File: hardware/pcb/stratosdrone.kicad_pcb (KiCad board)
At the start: 4 copper layers, 36 x 70 mm, 115 parts, among them J1 BATT_PH2, J10 DBG, J11 C6DBG, J2 USB-C-16P, J3 FLOW_HDR, J4 CAM_FFC15, J5 MOTOR1, J6 MOTOR2, J7 MOTOR3, J8 MOTOR4, J9 EXP, Q1 AO3400A, Q2 AO3400A, Q3 AO3400A, Q4 AO3400A, SW1 RESET, SW2 BOOT, U1 ESP32-P4NRW32, U10 TLV62569DBVR, U2 W25Q128JVSIQ, U3 ESP32-C6-MINI-1, U4 TP4056-42-ESOP8, U5 SY8089AAAC, U6 ICM-42688-P, U7 SPL06-001, U8 VL53L1X, U9 PMW3901MB, Y1 40MHz

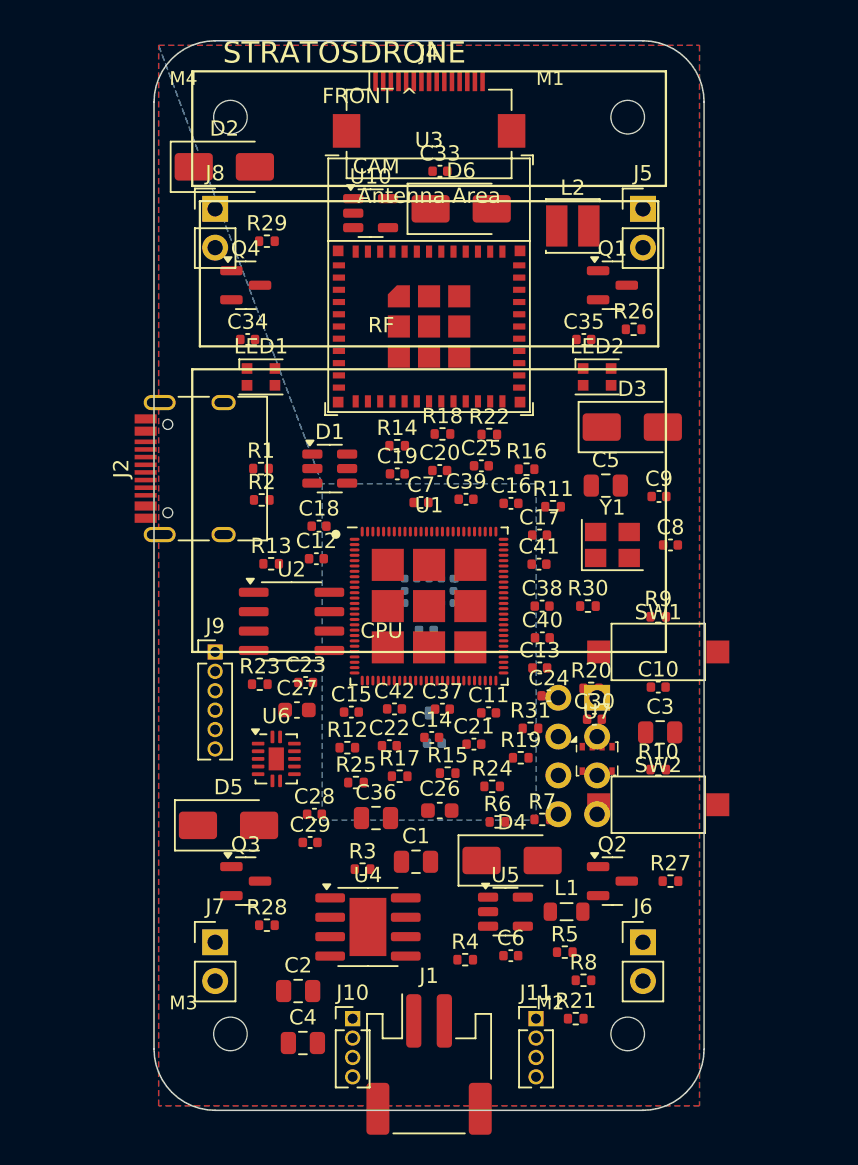
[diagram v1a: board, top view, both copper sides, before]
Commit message: hardware/pcb: fix two router-blocking footprint bugs + add autoroute pipeline
Two real bugs that broke Specctra DSN export and any autorouter, found while
building the AI-assisted routing flow:

1. Mounting holes had EMPTY references. gen_pcb.py created the 4 corner M2 NPTH
   holes as footprints with no reference designator; Specctra export aborts when
   multiple components share an empty ref, so ExportSpecctraDSN() returned False
   with no error. Now MH1..MH4 with a real footprint id, excluded from BOM/CPL.

2. U9 (PMW3901) placeholder had all 8 pads stacked at (0,0) on 8 DIFFERENT nets
   (GND/3V3/SPI_*/CS_FLOW) — a hard short that poisoned the maze router for those
   nets. Replaced with a spread 2x4 DFN-style land (0.8mm pitch); verified zero
   different-net pad overlaps remain board-wide.

New routing infrastructure:
- scripts/route_board.py: export Specctra DSN (drops outer F.Cu/B.Cu pours so
  signal layers are free, marks inner In1/In2 as power planes, optional
  power-net strip), drive Freerouting headless under xvfb, import the routed
  SES back with a self-contained parser (correct um scale + Specctra Y-flip),
  and stitch power pads to their planes.
- ROUTING.md: method + online-AI (DeepPCB) and Windows-Freerouting fallbacks.
- stratosdrone.dsn: committed handoff so the board can be routed anywhere.

Board regenerated; check_consistency passes. Signal autoroute itself is still
in progress (see ROUTING.md); these fixes unblock it on every router.

Co-Authored-By: Claude Opus 4.8 <noreply@anthropic.com>
Claude-Session: https://claude.ai/code/session_011szEEHZ8KTTsZmGFgY6Cjw
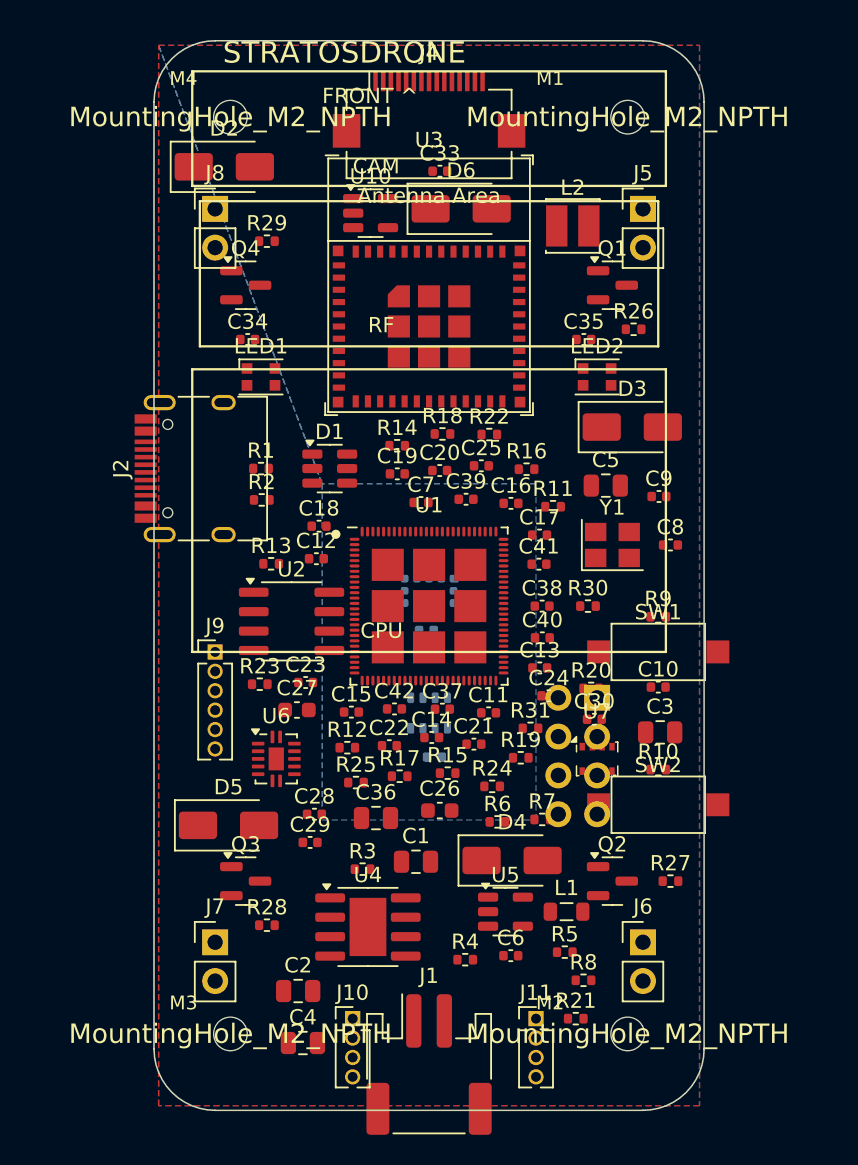
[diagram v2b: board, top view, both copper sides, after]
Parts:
- removed ? (x4): , 
- added MH1: MountingHole_M2_NPTH, MountingHole:MountingHole_2.2mm_M2, F.Cu at (5.00, 5.00)
- added MH2: MountingHole_M2_NPTH, MountingHole:MountingHole_2.2mm_M2, F.Cu at (5.00, 65.0)
- added MH3: MountingHole_M2_NPTH, MountingHole:MountingHole_2.2mm_M2, F.Cu at (31.0, 5.00)
- added MH4: MountingHole_M2_NPTH, MountingHole:MountingHole_2.2mm_M2, F.Cu at (31.0, 65.0)
- moved C32 0.91 mm to (18.3, 46.9)

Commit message: hardware/pcb: apply AI signal autoroute (Freerouting 1.9), ~89% of signals
Drove Freerouting 1.9.0 headless (xvfb) via scripts/route_board.py on the
de-bugged board and imported the result: 295 signal track segments on
F.Cu/B.Cu (stratosdrone.ses, committed). The self-contained SES importer was
fixed to the correct Specctra scale (0.1um/unit) and Y-axis flip, verified
against known pad positions.

State: signal nets ~89% routed; the rest is finished in KiCad (see ROUTING.md
and KNOWN_GAPS item 1):
- fill the 4 copper zones (hotkey B) -> connects same-layer GND/VBAT pads;
- add cross-layer power stitch vias (3V3 -> In2 plane) — connect_power() does
  a first pass but headless zone-fill can't replicate KiCad's GUI connectivity
  reliably, so KiCad's fill is authoritative;
- route the few remaining ratsnest signals; re-export gerbers.

Why not 100% here: this dense 36x70mm 2-signal-layer board caps at ~62% of
all connections per autorouter pass in this sandbox (FR1.9 best; FR2.1 weaker;
both plateau). A full clean route wants more compute — route the committed
stratosdrone.dsn on DeepPCB.ai (cloud AI) or Windows Freerouting and re-import
with `route_board.py --skip-route`.

`make board` regenerates the UNROUTED board; re-apply with
`route_board.py --skip-route`. check_consistency passes.

Co-Authored-By: Claude Opus 4.8 <noreply@anthropic.com>
Claude-Session: https://claude.ai/code/session_011szEEHZ8KTTsZmGFgY6Cjw
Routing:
- net VBAT: track 0.00 -> 130.0 mm
- net GND: track 0.00 -> 62.7 mm
- net SPI_MISO: track 0.00 -> 26.1 mm, vias 0 -> 1
- net VBUS: track 0.00 -> 24.9 mm
- net SPI_MOSI: track 0.00 -> 23.6 mm, vias 0 -> 1
- net LED_D12: track 0.00 -> 21.8 mm, vias 0 -> 2
- net M3_GATE: track 0.00 -> 21.2 mm
- net I2C_SCL: track 0.00 -> 19.7 mm
- net SPI_SCLK: track 0.00 -> 19.3 mm, vias 0 -> 1
- net I2C_SDA: track 0.00 -> 17.1 mm
- net SDIO_D1: track 0.00 -> 16.8 mm
- net M1_D: track 0.00 -> 15.9 mm
- net FB_DCDC: track 0.00 -> 14.0 mm
- net M2_D: track 0.00 -> 13.0 mm
- net FB3V3: track 0.00 -> 12.1 mm
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
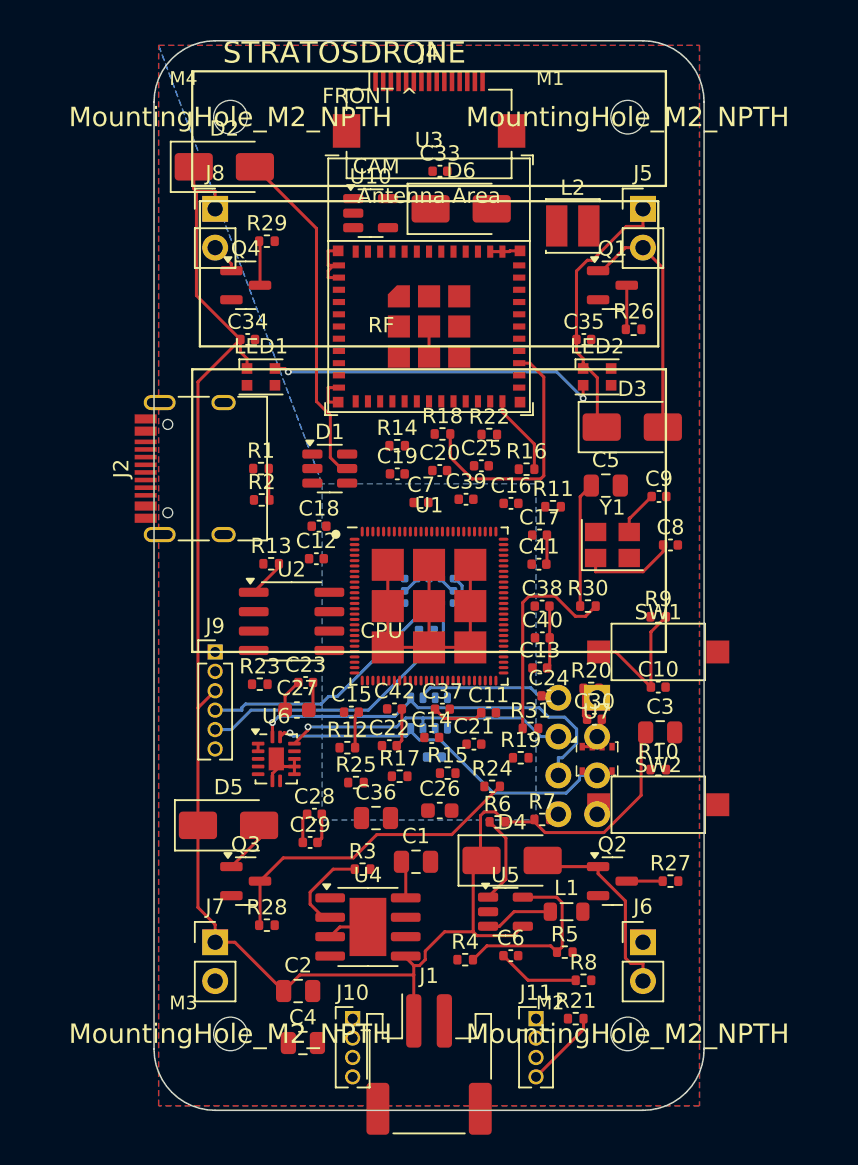
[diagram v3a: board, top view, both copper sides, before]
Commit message: hardware/pcb: fix component placement — nothing off-board, no overlaps
Opening the board in KiCad showed parts hanging off the outline (USB-C J2,
the reset/boot switches SW1/SW2) and a congested bottom-right cluster. Root
cause: phase-1 anchors in the PLACE table were positioned by hand with no
boundary/overlap check, and the phase-3 repair pass explicitly skips anything
in PLACE — so off-board or colliding *major* parts were never corrected.

Placement fixes (PLACE table):
- SW1/SW2 (9.3mm slide switches) rotated 90° and moved to a clear vertical
  column on the right edge — they no longer hang 1.6mm off the edge nor
  collide with U7/J3 and their gate resistors (the bottom-right mess).
- J2 USB-C moved right so all contacts sit on-board (the 90° rotation made the
  1.45mm contact fingers straddle the x=0 edge -> off-board copper).
- J1 battery JST pulled up off the bottom edge; J10/J11 UART pads likewise.
- U3 (ESP32-C6) spaced from the camera FFC; U4/U5/L1 nudged for clearance.

Engine: add assert_placement(), run at the end of main(), which loads the
saved board and reports any pad outside the outline (hard error -> exit 2) and
significant same-side courtyard overlaps (warnings). `make board` now fails if
placement regresses off-board.

Result: all 111 footprints inside the 36x70 outline, zero same-side pad
overlaps, tightest body gap 0.28mm (JLCPCB-safe). Remaining courtyard warnings
are oversized module IPC courtyards (ESP32-C6/camera-FFC/USB-C) with >=0.28mm
real clearance.

Note: moving parts invalidates the previous autoroute; tracks are re-routed on
the corrected placement in a follow-up commit. stratosdrone.dsn re-exported.

Co-Authored-By: Claude Opus 4.8 <noreply@anthropic.com>
Claude-Session: https://claude.ai/code/session_011szEEHZ8KTTsZmGFgY6Cjw
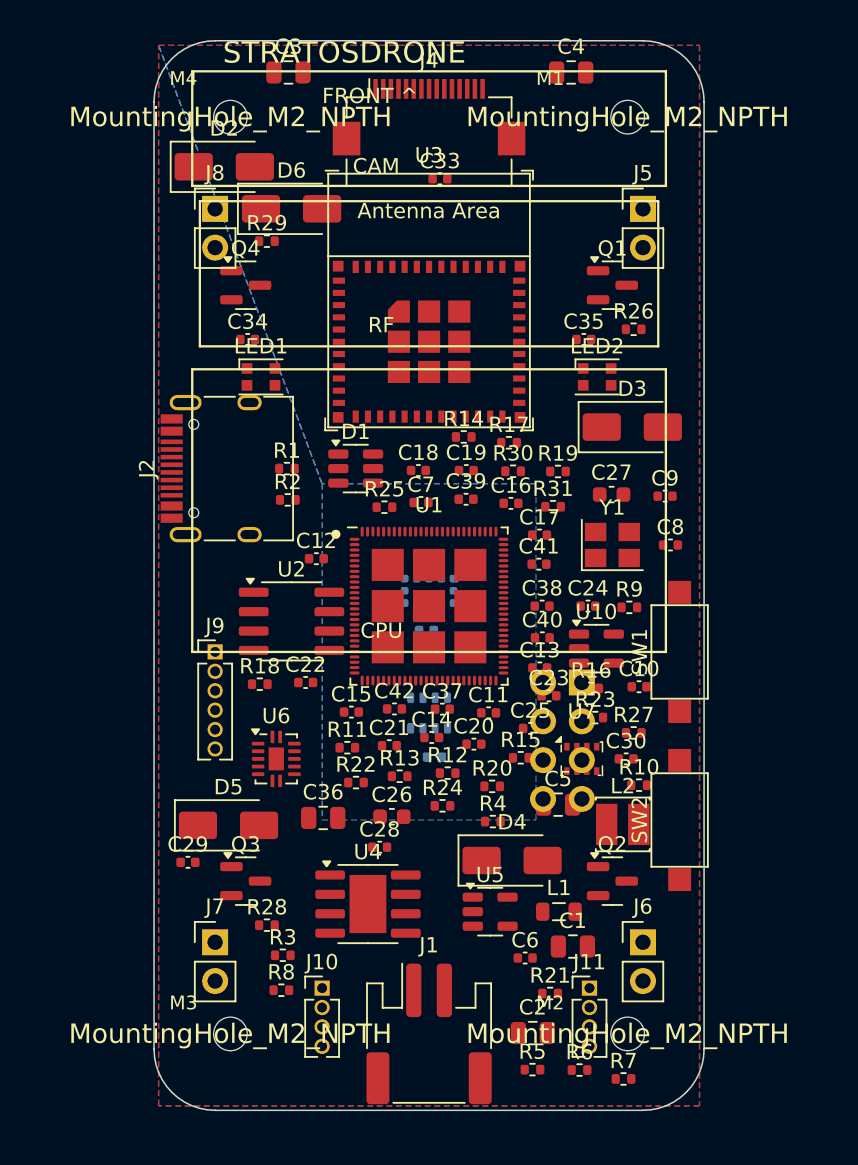
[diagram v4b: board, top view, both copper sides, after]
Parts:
- moved C4 65.9 mm to (27.3, 2.08)
- moved C3 49.6 mm to (8.80, 2.08)
- moved L2 39.3 mm to (30.7, 51.3)
- moved U10 32.1 mm to (29.0, 39.8)
- moved C27 25.0 mm to (29.9, 29.7)
- moved R22 24.4 mm to (13.2, 48.5)
- moved R17 23.0 mm to (23.2, 26.3)
- moved R23 22.1 mm to (28.9, 44.3)
- moved C5 21.1 mm to (26.4, 50.0)
- moved R11 20.7 mm to (12.7, 46.3)
- moved R18 20.3 mm to (6.92, 42.1)
- moved R8 19.8 mm to (8.33, 62.1)
- moved R19 18.9 mm to (26.4, 28.2)
- moved R25 18.1 mm to (15.1, 30.5)
- moved C20 18.0 mm to (20.9, 46.0)
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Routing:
- net VBAT: track 130.0 -> 0.00 mm
- net GND: track 62.7 -> 0.00 mm
- net SPI_MISO: track 26.1 -> 0.00 mm, vias 1 -> 0
- net VBUS: track 24.9 -> 0.00 mm
- net SPI_MOSI: track 23.6 -> 0.00 mm, vias 1 -> 0
- net LED_D12: track 21.8 -> 0.00 mm, vias 2 -> 0
- net M3_GATE: track 21.2 -> 0.00 mm
- net I2C_SCL: track 19.7 -> 0.00 mm
- net SPI_SCLK: track 19.3 -> 0.00 mm, vias 1 -> 0
- net I2C_SDA: track 17.1 -> 0.00 mm
- net SDIO_D1: track 16.8 -> 0.00 mm
- net M1_D: track 15.9 -> 0.00 mm
- net FB_DCDC: track 14.0 -> 0.00 mm
- net M2_D: track 13.0 -> 0.00 mm
- net FB3V3: track 12.1 -> 0.00 mm
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
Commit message: hardware/pcb: re-route on corrected placement (Freerouting 1.9)
The placement fix moved components, invalidating the previous autoroute, so the
board is re-routed from a freshly exported DSN that matches the new positions.

- Freerouting 1.9, 6 passes + optimization (headless under xvfb): 224 wires /
  27 vias -> 496 track segments + 27 vias imported onto F.Cu/B.Cu.
- connect_power(): 176 stitch vias seat GND/3V3/VBAT pads onto their planes.
- Zones filled; 14 gerbers + drill re-exported to jlcpcb/gerbers/.

Connectivity after fill+stitch: 99 ratsnest connections remain (221 pre-fill;
better than the prior placement's ~114). Remaining breaks are ~1/3 power
(cross-layer thermal links KiCad's GUI fill resolves) and ~2/3 signal nets the
dense 2-signal-layer stackup couldn't finish headless. Finish in KiCad (re-fill
zones, route remaining ratsnest) or re-route stratosdrone.dsn with more compute.
KNOWN_GAPS item 1 updated with the new numbers.

Co-Authored-By: Claude Opus 4.8 <noreply@anthropic.com>
Claude-Session: https://claude.ai/code/session_011szEEHZ8KTTsZmGFgY6Cjw
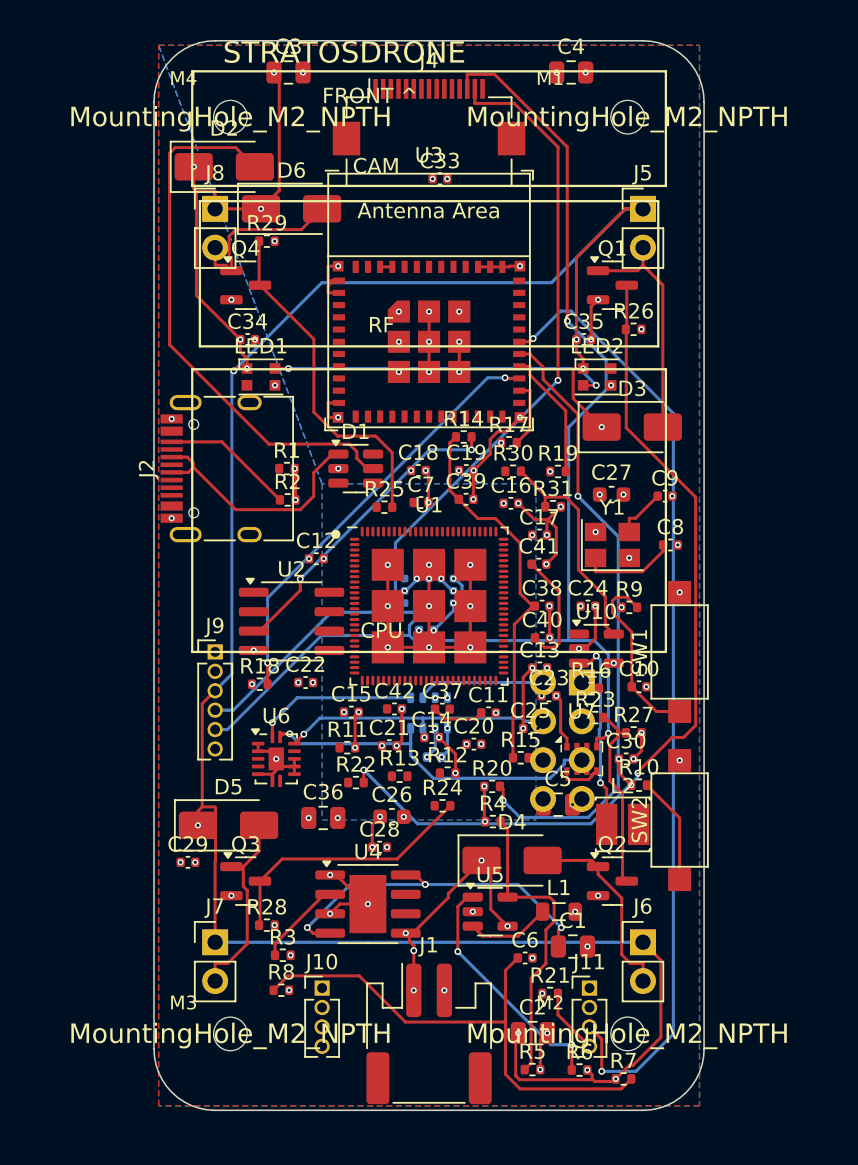
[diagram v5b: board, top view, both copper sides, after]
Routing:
- net VBAT: track 0.00 -> 186.1 mm, vias 0 -> 23
- net GND: track 0.00 -> 99.5 mm, vias 0 -> 112
- net I2C_SCL: track 0.00 -> 82.7 mm, vias 0 -> 2
- net C6_U0RXD: track 0.00 -> 63.2 mm, vias 0 -> 2
- net I2C_SDA: track 0.00 -> 59.4 mm, vias 0 -> 1
- net VBUS: track 0.00 -> 59.2 mm, vias 0 -> 3
- net M1_GATE: track 0.00 -> 57.6 mm, vias 0 -> 2
- net SDIO_D3: track 0.00 -> 41.3 mm, vias 0 -> 2
- net VBAT_SENSE: track 0.00 -> 33.7 mm
- net SDIO_D1: track 0.00 -> 28.1 mm, vias 0 -> 2
- net VDD_FLASHIO: track 0.00 -> 24.8 mm
- net SPI_MOSI: track 0.00 -> 23.2 mm, vias 0 -> 1
- net M4_GATE: track 0.00 -> 22.5 mm
- net LED_D12: track 0.00 -> 22.3 mm, vias 0 -> 2
- net 3V3: track 0.00 -> 20.6 mm, vias 0 -> 43
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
